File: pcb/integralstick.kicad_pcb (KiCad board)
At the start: 4 copper layers, 210 parts, among them J1 CONN_INTEGRALSTICK_FPGA_DEVICE, J2 CONN_INTEGRALSTICK_MCU_DEVICE, Q1 SSM6N58NU, Q2 SSM6N58NU, Q3 SSM6N58NU, U1 STM32F777NIH6‎, U2 XC7A50T-1FTG256C, U3 S27KS0641, U4 S27KS0641, U5 KSZ9031RN, U6 S25FL064LABNFI011‎, U7 LTC3374-QFN

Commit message: Initial design rules
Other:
- net class Default: clearance 0.125 -> 0.1; trace_width 0.125 -> 0.1; via_dia 0.6 -> 0.46; via_drill 0.254 -> 0.25
- rule trace_clearance: 0.125 -> 0.1
- rule trace_min: 0.125 -> 0.1
- rule via_min_drill: 0.254 -> 0.25
- rule via_min_size: 0.458 -> 0.46
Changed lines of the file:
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@@
   )
   (setup
-    (last_trace_width 0.125)
-    (user_trace_width 0.125)
-    (user_trace_width 0.25)
-    (user_trace_width 0.328)
-    (trace_clearance 0.125)
+    (last_trace_width 0.1)
+    (user_trace_width 0.1)
+    (user_trace_width 0.165)
+    (user_trace_width 0.175)
+    (trace_clearance 0.1)
     (zone_clearance 0.508)
     (zone_45_only no)
-    (trace_min 0.125)
-    (via_size 0.6)
-    (via_drill 0.254)
-    (via_min_size 0.458)
-    (via_min_drill 0.254)
-    (user_via 0.458 0.254)
-    (user_via 0.6 0.254)
+    (trace_min 0.1)
+    (via_size 0.46)
+    (via_drill 0.25)
+    (via_min_size 0.46)
+    (via_min_drill 0.25)
+    (user_via 0.46 0.25)
     (uvia_size 0.3)
     (uvia_drill 0.1)
@@
   (net 392 /FPGA/GPIO_LED3)
   (net_class Default "This is the default net class."
-    (clearance 0.125)
-    (trace_width 0.125)
-    (via_dia 0.6)
-    (via_drill 0.254)
+    (clearance 0.1)
+    (trace_width 0.1)
+    (via_dia 0.46)
+    (via_drill 0.25)
     (uvia_dia 0.3)
     (uvia_drill 0.1)
-    (diff_pair_width 0.245)
-    (diff_pair_gap 0.25)
+    (diff_pair_width 0.165)
+    (diff_pair_gap 0.1)
     (add_net /1V0)
     (add_net /1V2)

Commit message: Finished initial footprint assignments
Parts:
- added C46: CPH3225A-2K, azonenberg_pcb:CAP_SEIKO_CPH3225A, F.Cu at (108.6, 66.7)
- added D2: CTS520,L3F‎, azonenberg_pcb:SOD882, F.Cu at (112.5, 65.5)
- added FB1: 600R @ 100 MHz, azonenberg_pcb:EIA_0402_CAP_NOSILK, F.Cu at (117.9, 67.9)
- added FB2: 600R @ 100 MHz, azonenberg_pcb:EIA_0402_CAP_NOSILK, F.Cu at (120.8, 65.4)
- added FB3: 600R @ 100 MHz, azonenberg_pcb:EIA_0402_CAP_NOSILK, F.Cu at (120.4, 67.9)
- added U10: DSC6083MI2A-032K768, azonenberg_pcb:OSCILLATOR_2.0x1.6, F.Cu at (117.7, 74.6)
- added U12: DSC6001HI2A-025.0000‎, azonenberg_pcb:OSCILLATOR_1.6x1.2, F.Cu at (111.2, 73.5)
- added U8: DSC6001HI2A-025.0000, azonenberg_pcb:OSCILLATOR_1.6x1.2, F.Cu at (118.3, 65.8)
- added U9: AT24MAC402-UDFN, azonenberg_pcb:DFN_8_0.5MM_2x3MM, F.Cu at (107.5, 74.2)
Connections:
- R21 pad 2: Net-(R21-Pad2) -> (no net)
- R27 pad 2: Net-(R27-Pad2) -> (no net)
- R45 pad 1: Net-(D2-Pad1) -> (no net)
- R7 pad 1: Net-(R7-Pad1) -> (no net)
- U1 pad B10: Net-(U1-PadB10) -> (no net)
- U1 pad B3: Net-(U1-PadB3) -> (no net)
- U1 pad B7: Net-(U1-PadB7) -> (no net)
- U1 pad B8: Net-(U1-PadB8) -> (no net)
- U1 pad B9: Net-(U1-PadB9) -> (no net)
- U1 pad C13: Net-(U1-PadC13) -> (no net)
- U1 pad C14: Net-(U1-PadC14) -> (no net)
- U1 pad C2: Net-(U1-PadC2) -> (no net)
- U1 pad C3: Net-(U1-PadC3) -> (no net)
- U1 pad C4: Net-(U1-PadC4) -> (no net)
- U1 pad C5: Net-(U1-PadC5) -> (no net)
- U1 pad C6: Net-(U1-PadC6) -> (no net)
- U1 pad C7: Net-(U1-PadC7) -> (no net)
- U1 pad C8: Net-(U1-PadC8) -> (no net)
- U1 pad C9: Net-(U1-PadC9) -> (no net)
- U1 pad D10: Net-(U1-PadD10) -> (no net)
- U1 pad D13: Net-(U1-PadD13) -> (no net)
- U1 pad D14: Net-(U1-PadD14) -> (no net)
- U1 pad D3: Net-(U1-PadD3) -> (no net)
- U1 pad D4: Net-(U1-PadD4) -> (no net)
- U1 pad D5: Net-(U1-PadD5) -> (no net)
- U1 pad D6: Net-(U1-PadD6) -> (no net)
- U1 pad D7: Net-(U1-PadD7) -> (no net)
- U1 pad D8: Net-(U1-PadD8) -> (no net)
- U1 pad E12: Net-(U1-PadE12) -> (no net)
- U1 pad E13: Net-(U1-PadE13) -> (no net)
- U1 pad E14: Net-(U1-PadE14) -> (no net)
- U1 pad E3: Net-(U1-PadE3) -> (no net)
- U1 pad E4: Net-(U1-PadE4) -> (no net)
- U1 pad F1: Net-(U1-PadF1) -> (no net)
- U1 pad F12: Net-(U1-PadF12) -> (no net)
- U1 pad F13: Net-(U1-PadF13) -> (no net)
- U1 pad F3: Net-(U1-PadF3) -> (no net)
- U1 pad G12: Net-(U1-PadG12) -> (no net)
- U1 pad G13: Net-(U1-PadG13) -> (no net)
- U1 pad G3: Net-(U1-PadG3) -> (no net)
- U1 pad G4: Net-(U1-PadG4) -> (no net)
- U1 pad H1: Net-(U1-PadH1) -> (no net)
- U1 pad H12: Net-(U1-PadH12) -> (no net)
- U1 pad H13: Net-(U1-PadH13) -> (no net)
- U1 pad H14: Net-(U1-PadH14) -> (no net)
- U1 pad H3: Net-(U1-PadH3) -> (no net)
- U1 pad H4: Net-(U1-PadH4) -> (no net)
- U1 pad J12: Net-(U1-PadJ12) -> (no net)
- U1 pad J13: Net-(U1-PadJ13) -> (no net)
- U1 pad J14: Net-(U1-PadJ14) -> (no net)
- U1 pad J15: Net-(U1-PadJ15) -> (no net)
- U1 pad J4: Net-(U1-PadJ4) -> (no net)
- U1 pad K12: Net-(U1-PadK12) -> (no net)
- U1 pad K4: Net-(U1-PadK4) -> (no net)
- U1 pad L1: Net-(U1-PadL1) -> (no net)
- U1 pad M12: Net-(U1-PadM12) -> (no net)
- U1 pad M13: Net-(U1-PadM13) -> (no net)
- U1 pad M14: Net-(U1-PadM14) -> (no net)
- U1 pad M15: Net-(U1-PadM15) -> (no net)
- U1 pad M6: Net-(U1-PadM6) -> (no net)
- U1 pad M7: Net-(U1-PadM7) -> (no net)
- U1 pad M8: Net-(U1-PadM8) -> (no net)
- U1 pad M9: Net-(U1-PadM9) -> (no net)
- U1 pad N11: Net-(U1-PadN11) -> (no net)
- U1 pad N12: Net-(U1-PadN12) -> (no net)
- U1 pad N14: Net-(U1-PadN14) -> (no net)
- U1 pad N15: Net-(U1-PadN15) -> (no net)
- U1 pad N6: Net-(U1-PadN6) -> (no net)
- U1 pad N7: Net-(U1-PadN7) -> (no net)
- U1 pad N8: Net-(U1-PadN8) -> (no net)
- U1 pad P14: Net-(U1-PadP14) -> (no net)
- U1 pad P15: Net-(U1-PadP15) -> (no net)
- U1 pad P6: Net-(U1-PadP6) -> (no net)
- U1 pad P7: Net-(U1-PadP7) -> (no net)
- U1 pad R6: Net-(U1-PadR6) -> (no net)
- U1 pad R7: Net-(U1-PadR7) -> (no net)
- U2 pad F14: Net-(U2-PadF14) -> (no net)
- U2 pad G11: Net-(U2-PadG11) -> (no net)
- U2 pad G14: Net-(U2-PadG14) -> (no net)
- U2 pad G16: Net-(U2-PadG16) -> (no net)
- U2 pad H13: Net-(U2-PadH13) -> (no net)
- U2 pad H16: Net-(U2-PadH16) -> (no net)
- U2 pad H8: Net-(U2-PadH8) -> (no net)
- U2 pad J15: Net-(U2-PadJ15) -> (no net)
- U2 pad J16: Net-(U2-PadJ16) -> (no net)
- U2 pad J7: Net-(U2-PadJ7) -> (no net)
- U5 pad 13: Net-(U5-Pad13) -> (no net)
- U5 pad 38: Net-(U5-Pad38) -> (no net)
- U5 pad 43: Net-(U5-Pad43) -> (no net)
- U5 pad 45: Net-(U5-Pad45) -> (no net)
- U5 pad 47: Net-(U5-Pad47) -> (no net)

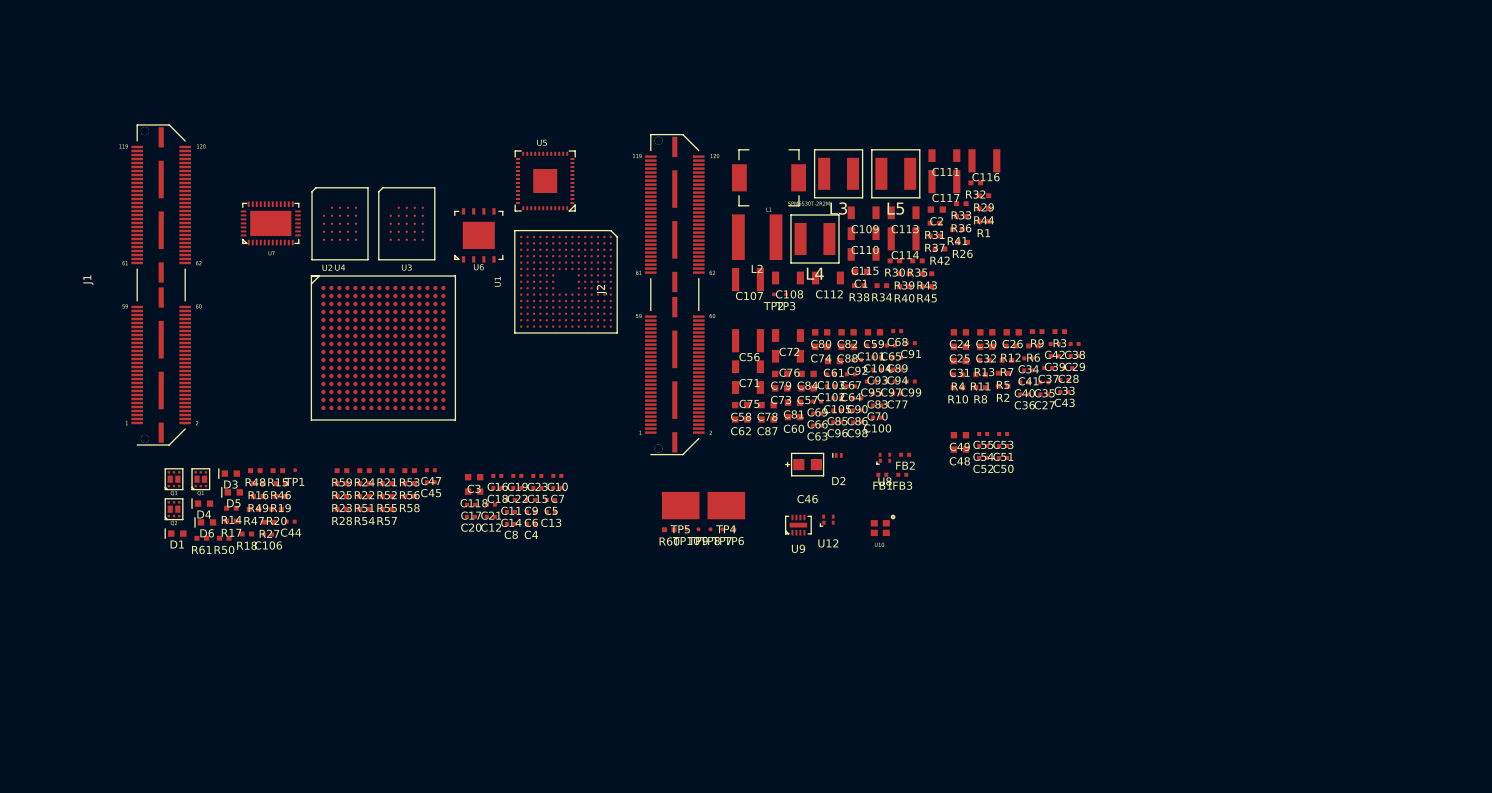
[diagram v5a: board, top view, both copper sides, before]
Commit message: Initial work on FPGA fanout
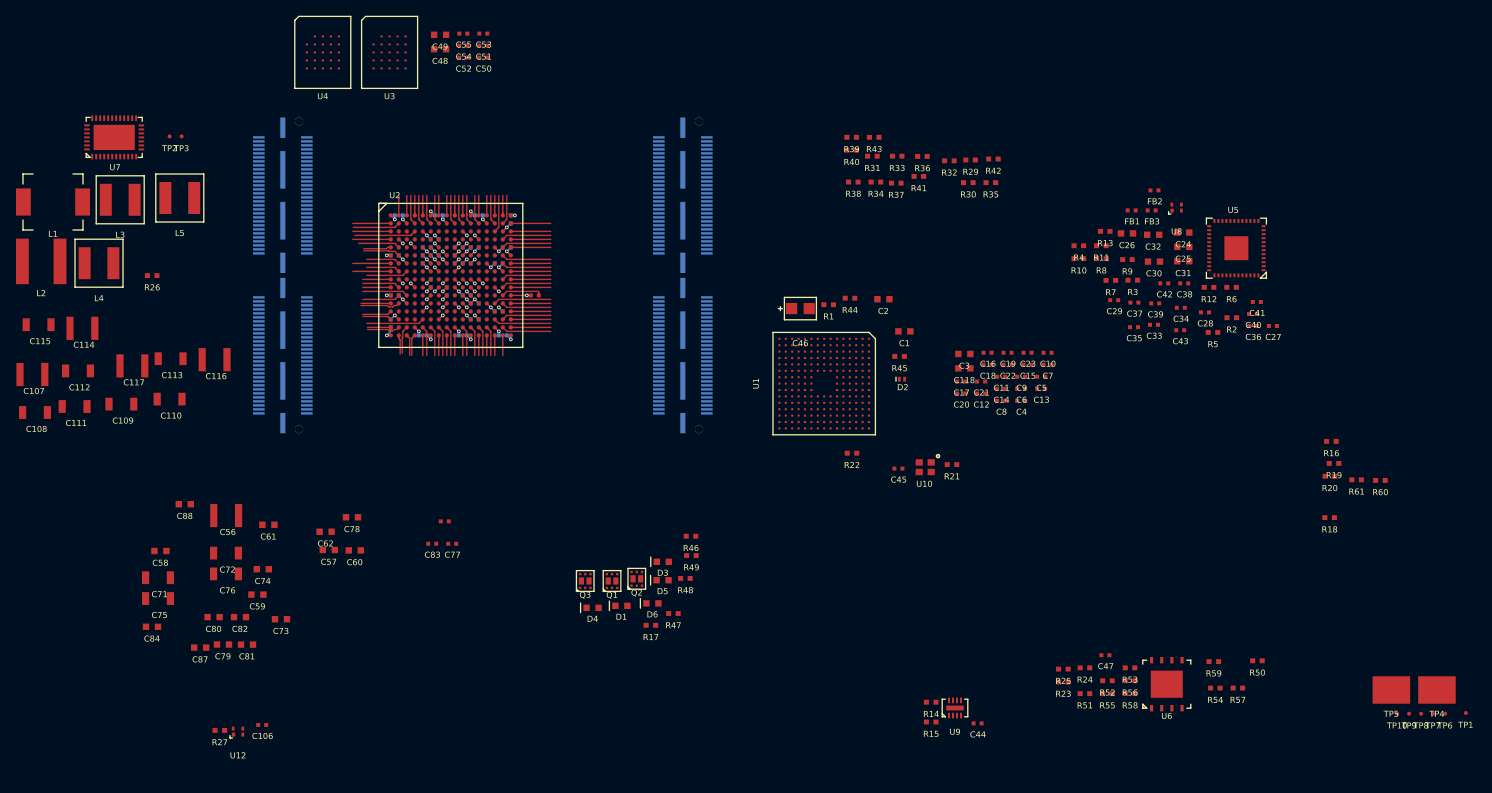
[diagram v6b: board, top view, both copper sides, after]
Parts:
- C100, C101, C102, C103, C105, C63, C64, C65, C66, C67, C68, C69, C70, C85, C86, C89, C90, C91, C92, C93, C94, C95, C96, C97, C98, C99, J1, J2: moved to B.Cu
- R28: footprint azonenberg_pcb:EIA_0402_RES_NOSILK -> azonenberg_pcb:EIA_0402_CAP_NOSILK
- moved TP1 149.4 mm to (190.9, 97.7)
- moved R61 144.5 mm to (177.2, 68.5)
- moved R18 135.4 mm to (173.9, 73.3)
- moved R16 134.2 mm to (174.1, 63.8)
- moved R19 131.7 mm to (174.4, 66.5)
- moved R20 131.7 mm to (173.9, 68.1)
- moved R50 130.0 mm to (164.8, 91.2)
- moved C111 113.2 mm to (17.0, 59.4)
- moved R59 111.6 mm to (159.4, 91.3)
- moved R54 108.7 mm to (159.6, 94.6)
- moved R57 108.7 mm to (162.4, 94.6)
- moved C117 104.1 mm to (24.2, 54.3)
- moved C115 103.5 mm to (12.5, 49.1)
- moved C114 103.3 mm to (17.9, 49.6)
- moved U6 102.7 mm to (153.5, 94.1)
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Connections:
- R21 pad 2: (no net) -> Net-(R21-Pad2)
- R27 pad 2: (no net) -> Net-(R27-Pad2)
- R45 pad 1: (no net) -> Net-(D2-Pad1)
- R7 pad 1: (no net) -> Net-(R7-Pad1)
- U10 pad 3: Net-(U10-Pad3) -> (no net)
- U2 pad A13: /FPGA/IO_3V3_12 -> /FPGA/IO_3V3_14
- U2 pad A14: /FPGA/IO_3V3_13 -> /FPGA/IO_3V3_25
- U2 pad C12: /FPGA/IO_3V3_22 -> (no net)
- U2 pad C14: /FPGA/IO_3V3_14 -> /FPGA/IO_3V3_22
- U2 pad D14: /FPGA/IO_3V3_25 -> (no net)
- U2 pad F13: /FPGA/IO_3V3_20 -> (no net)
- U2 pad G16: (no net) -> /FPGA/I2C_SCL
- U2 pad H14: /FPGA/I2C_SCL -> (no net)
- U2 pad H16: (no net) -> /FPGA/IO_3V3_20
- U2 pad J15: (no net) -> /FPGA/IO_3V3_12
- U2 pad J16: (no net) -> /FPGA/IO_3V3_13
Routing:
- net /GND: track 0.00 -> 42.9 mm, vias 0 -> 38
- net /3V3: track 0.00 -> 17.0 mm, vias 0 -> 15
- net /1V8: track 0.00 -> 12.6 mm, vias 0 -> 12
- net /1V0: track 0.00 -> 12.0 mm, vias 0 -> 9
- net /RAM/RAM1_DQ7: track 0.00 -> 7.71 mm
- net /MCU/RMII_TXD1: track 0.00 -> 7.21 mm
- net /FPGA/GPIO_2V5_1: track 0.00 -> 7.21 mm
- net /Ethernet/RGMII_RX_DV: track 0.00 -> 7.21 mm
- net Net-(R57-Pad1): track 0.00 -> 6.21 mm
- net /MCU/RMII_TX_EN: track 0.00 -> 6.21 mm
- net /MCU/DCMI_VSYNC: track 0.00 -> 6.21 mm
- net /FPGA/IO_3V3_29: track 0.00 -> 6.21 mm
- net /FPGA/IO_3V3_26: track 0.00 -> 6.21 mm
- net /FPGA/IO_3V3_12: track 0.00 -> 6.21 mm
- net /FPGA/I2C_SDA: track 0.00 -> 6.21 mm
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
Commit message: Finished first iteration layout of RAM. Lots of pin swaps.
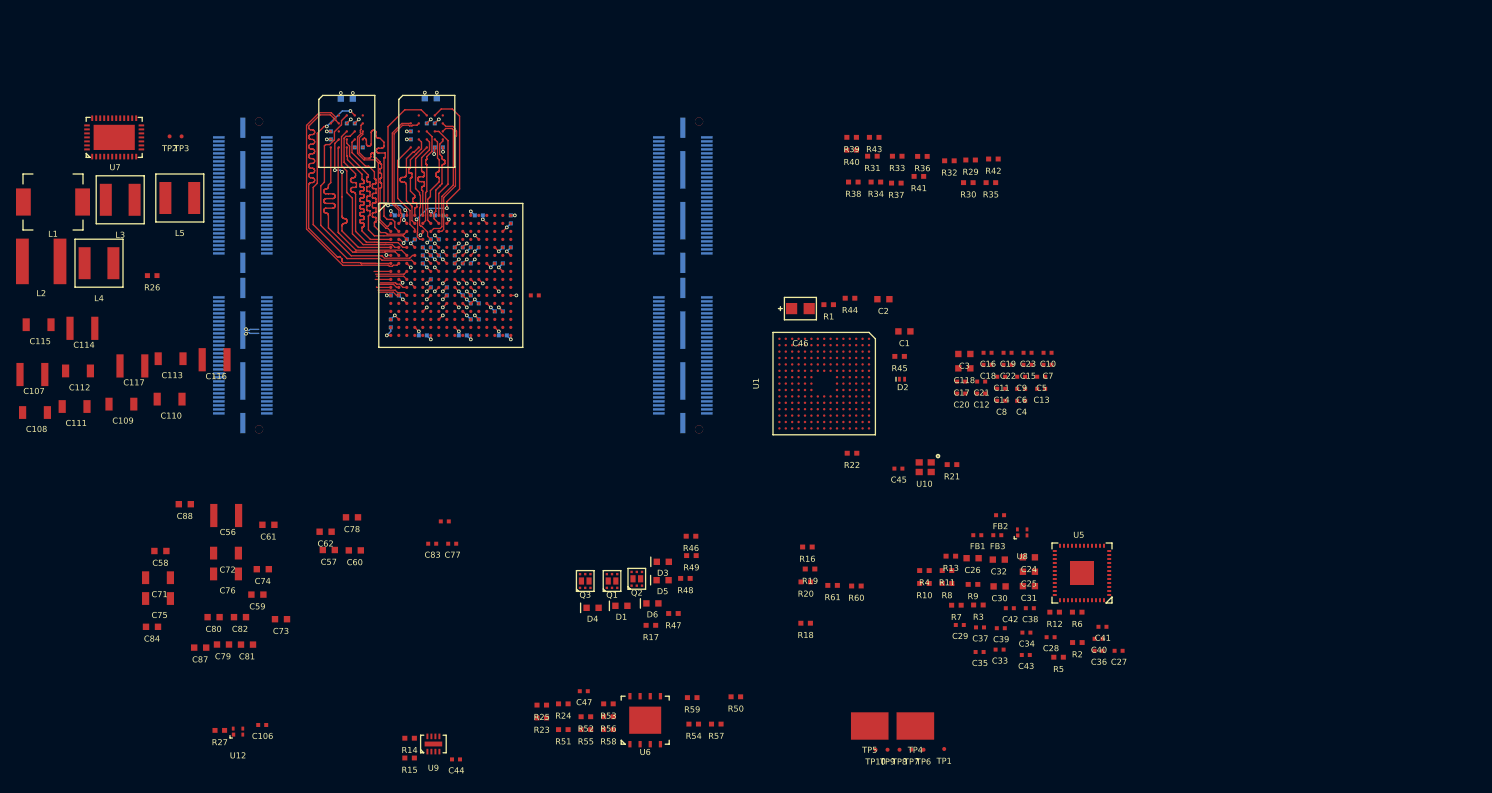
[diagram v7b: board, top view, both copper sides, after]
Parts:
- C48, C49, C50, C51, C52, C53, C54, C55: moved to B.Cu
- U2: footprint azonenberg_pcb:BGA_256_17x17_FULLARRAY_1MM -> azonenberg_pcb:BGA_256_17x17_FULLARRAY_1MM_0.4MM_FTG256
- moved R19 66.8 mm to (108.9, 79.7)
- moved R20 66.8 mm to (108.4, 81.3)
- moved R18 66.8 mm to (108.4, 86.5)
- moved R61 66.8 mm to (111.7, 81.8)
- moved R16 66.8 mm to (108.6, 77.0)
- moved R60 66.8 mm to (114.7, 81.8)
- moved R53 65.4 mm to (83.7, 96.6)
- moved R56 65.4 mm to (83.7, 98.2)
- moved R58 65.4 mm to (83.7, 99.8)
- moved TP4 65.4 mm to (122.1, 99.3)
- moved R23 65.4 mm to (75.4, 98.3)
- moved R24 65.4 mm to (78.1, 96.6)
- moved R25 65.4 mm to (75.4, 96.7)
- moved R50 65.4 mm to (99.6, 95.7)
- moved R51 65.4 mm to (78.1, 99.8)
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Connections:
- J1 pad 42: /FPGA/LVDS_DQ3_P -> /FPGA/LVDS_DQ3_N
- J1 pad 44: /FPGA/LVDS_DQ3_N -> /FPGA/LVDS_DQ3_P
- U2 pad A2: /RAM/RAM1_DQ0 -> /RAM/RAM0_CK_N
- U2 pad A3: /RAM/RAM0_DQ7 -> /RAM/RAM0_CS_N
- U2 pad A4: /RAM/RAM0_DQ5 -> /RAM/RAM0_DQ1
- U2 pad A5: /RAM/RAM0_DQ4 -> /RAM/RAM0_DQ0
- U2 pad A7: /RAM/RAM0_DQ1 -> /RAM/RAM0_DQ2
- U2 pad B1: /RAM/RAM1_DQ2 -> /RAM/RAM1_PSC_N
- U2 pad B2: /RAM/RAM1_DQS -> /RAM/RAM0_CK_P
- U2 pad B5: /RAM/RAM0_DQ3 -> /RAM/RAM0_DQS
- U2 pad B6: /RAM/RAM0_DQ2 -> /RAM/RAM0_DQ3
- U2 pad B7: /RAM/RAM0_DQ0 -> /RAM/RAM0_DQ4
- U2 pad C1: /RAM/RAM1_DQ1 -> /RAM/RAM1_PSC_P
- U2 pad C2: /RAM/RAM0_PSC_N -> /RAM/RAM1_DQ4
- U2 pad C3: /RAM/RAM0_PSC_P -> /RAM/RAM1_DQ3
- U2 pad C4: /RAM/RAM1_DQ7 -> /RAM/RAM0_DQ7
- U2 pad C6: /RAM/RAM0_RST_N -> /RAM/RAM0_PSC_N
- U2 pad C7: /RAM/RAM0_CS_N -> /RAM/RAM0_PSC_P
- U2 pad D1: /RAM/RAM1_DQ4 -> /RAM/RAM1_DQ5
- U2 pad D3: /RAM/RAM1_DQ6 -> /RAM/RAM1_DQ0
- U2 pad D5: /RAM/RAM0_CK_N -> /RAM/RAM0_RST_N
- U2 pad D6: /RAM/RAM0_CK_P -> /RAM/RAM0_DQ5
- U2 pad E1: /RAM/RAM1_PSC_N -> /RAM/RAM1_DQ1
- U2 pad E2: /RAM/RAM1_DQ3 -> /RAM/RAM1_DQS
- U2 pad E3: /RAM/RAM1_DQ5 -> /RAM/RAM1_DQ2
- U2 pad E5: /RAM/RAM1_CS_N -> /RAM/GPIO_1V8_0
- U2 pad E6: /RAM/RAM0_DQS -> /RAM/GPIO_1V8_1
- U2 pad F2: /RAM/RAM1_PSC_P -> /RAM/RAM1_DQ7
- U2 pad F3: /RAM/RAM1_CK_N -> /RAM/RAM1_DQ6
- U2 pad F4: /RAM/RAM1_CK_P -> /RAM/RAM1_CS_N
- U2 pad G1: /RAM/GPIO_1V8_2 -> /RAM/RAM1_CK_N
- U2 pad G2: /RAM/GPIO_1V8_1 -> /RAM/RAM1_CK_P
- U2 pad G4: /RAM/GPIO_1V8_0 -> /RAM/RAM1_RST_N
- U2 pad G5: /RAM/RAM1_RST_N -> /RAM/GPIO_1V8_2
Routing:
- net /RAM/RAM1_CK_N: track 0.00 -> 37.5 mm
- net /RAM/RAM1_RST_N: track 0.00 -> 32.4 mm, vias 0 -> 2
- net /RAM/RAM1_CK_P: track 0.00 -> 32.1 mm
- net /RAM/RAM1_CS_N: track 0.00 -> 29.0 mm
- net /RAM/RAM0_RST_N: track 0.00 -> 23.4 mm, vias 0 -> 2
- net /RAM/RAM1_DQ6: track 0.00 -> 20.4 mm
- net /RAM/RAM1_DQ5: track 0.00 -> 20.2 mm
- net /RAM/RAM0_CS_N: track 0.00 -> 19.0 mm, vias 0 -> 2
- net /RAM/RAM1_DQ2: track 4.75 -> 23.1 mm
- net /RAM/RAM1_DQ7: track 7.71 -> 25.9 mm
- net /RAM/RAM1_DQ0: track 2.50 -> 20.1 mm
- net /RAM/RAM0_PSC_P: track 0.00 -> 15.9 mm
- net /RAM/RAM0_PSC_N: track 0.00 -> 15.9 mm
- net /RAM/RAM0_CK_P: track 0.00 -> 15.4 mm
- net /RAM/RAM1_DQ4: track 4.75 -> 20.2 mm
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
